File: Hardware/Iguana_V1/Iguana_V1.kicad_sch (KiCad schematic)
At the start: 112 parts, among them J1 ON OFF, J11 Conn_Coaxial, J12 Conn_Coaxial, J13 HDR-3x1, J14 HDR-3x1, J15 ds18b20, J16 SHT31, J17 HDR-2x1, J18 OLED, J19 NPK/H Sensor, J3 BAT, J4 HDR-2x1, J7 USB_B_Micro, J8 Cap. Moisture Sensor, J9 Conn_01x02, Q1 Q_PMOS_GSD, Q3 Q_Dual_NPN_NPN_BRT_E1B1C2E2B2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, SW1 SW_DIP_x02, SW2 SW_DIP_x02, SW3 SW_DIP_x02, U1 DW01, U10 RV-8803, U11 RFM95W-915S2, U12 MAX3485, U2 TP4056, U3 MT3608, U4 FS8205A, U5 AP2112K-3.3, U6 AP2112K-3.3, U7 AP2112K-3.3, U8 CH340C, U9 ESP32-WROOM-32D

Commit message: adding relay and working on pcb
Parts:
- removed H1, H2, H3, H4, H5, H6, H7, H8: MountingHole, MountingHole:MountingHole_3.2mm_M3, symbol Mechanical:MountingHole
- removed J1: ON OFF, Connector_JST:JST_XH_B2B-XH-A_1x02_P2.50mm_Vertical, symbol IoWLabsConnectors:HDR-2x1
- removed J11: Conn_Coaxial, Connector_Coaxial:SMA_Samtec_SMA-J-P-X-ST-EM1_EdgeMount, symbol Connector:Conn_Coaxial
- removed J14: HDR-3x1, Jumper:SolderJumper-3_P1.3mm_Open_RoundedPad1.0x1.5mm_NumberLabels, symbol IoWLabsConnectors:HDR-3x1
- removed JP1, JP2: SolderJumper_2_Open, Jumper:SolderJumper-2_P1.3mm_Open_RoundedPad1.0x1.5mm, symbol Jumper:SolderJumper_2_Open
- removed R16, R17: 200, Resistor_SMD:R_0603_1608Metric, symbol IoWLabs:RES
- removed R29, R30: 2.2k, Resistor_SMD:R_0603_1608Metric, symbol IoWLabs:RES
- added C6: 4.7u, Capacitor_SMD:C_0805_2012Metric, symbol IoWLabs:C
- added D12: LED, LED_SMD:LED_0603_1608Metric, symbol Device:LED
- added D13: MRA4007T3G, Diode_SMD:D_SMA, symbol Diode:MRA4007T3G
- added D14: WS2812B, LED_SMD:LED_WS2812B_PLCC4_5.0x5.0mm_P3.2mm, symbol LED:WS2812B
- added D9: D_Schottky, Diode_SMD:D_SMA, symbol Device:D_Schottky
- added J18, J19, J3: IN, Connector_JST:JST_XH_B2B-XH-A_1x02_P2.50mm_Vertical, symbol IoWLabsConnectors:HDR-2x1
- added J8: ON OFF, Jumper:SolderJumper-2_P1.3mm_Open_RoundedPad1.0x1.5mm, symbol IoWLabsConnectors:HDR-2x1
- added K1: Relay_SPDT, Relay_THT:Relay_SPDT_SANYOU_SRD_Series_Form_C, symbol Relay:Relay_SPDT
- added Q2: Q_PMOS_GSD, Package_TO_SOT_SMD:SOT-23, symbol Device:Q_PMOS_GSD
- added Q4: MMBT3904, Package_TO_SOT_SMD:SOT-23, symbol Transistor_BJT:MMBT3904
- added R14: 10K, Resistor_SMD:R_0603_1608Metric, symbol IoWLabs:RES
- added R38: 330, Resistor_SMD:R_0603_1608Metric, symbol IoWLabs:RES
- added R39: 10, Resistor_SMD:R_0603_1608Metric, symbol IoWLabs:RES
- J1: renamed from J3; footprint IoWLabsConnectors:Tb-2x1-5p-TH-V -> Connector_JST:JST_XH_B2B-XH-A_1x02_P2.50mm_Vertical
- J13: renamed from J17; footprint Connector_PinHeader_2.54mm:PinHeader_1x02_P2.54mm_Vertical -> Jumper:SolderJumper-2_P1.3mm_Open_RoundedPad1.0x1.5mm
- J2: renamed from J4; footprint Jumper:SolderJumper-2_P1.3mm_Open_RoundedPad1.0x1.5mm -> Connector_PinHeader_2.54mm:PinHeader_1x02_P2.54mm_Vertical
- J4: renamed from J8; footprint Connector_JST:JST_EH_S3B-EH_1x03_P2.50mm_Horizontal -> Connector_JST:JST_XH_B3B-XH-A_1x03_P2.50mm_Vertical
- J5: renamed from J15; footprint Connector_JST:JST_EH_S3B-EH_1x03_P2.50mm_Horizontal -> Connector_JST:JST_XH_B3B-XH-A_1x03_P2.50mm_Vertical
- J6: renamed from J16; footprint Connector_JST:JST_EH_S4B-EH_1x04_P2.50mm_Horizontal -> Connector_JST:JST_XH_B4B-XH-A_1x04_P2.50mm_Vertical
- J7: renamed from J19; footprint Connector_JST:JST_EH_S4B-EH_1x04_P2.50mm_Horizontal -> Connector_JST:JST_XH_B4B-XH-A_1x04_P2.50mm_Vertical
- renumbered C6 to C7, D5 to D4, D6 to D5, D7 to D6, D8 to D7, D4 to D8, J18 to J10, J7 to J12, J9 to J14, J10 to J15, J12 to J17, J13 to J9, R11 to R10, R12 to R11, R13 to R12, R2 to R13, R32 to R15, R36 to R16, R14 to R17, R33 to R18, R34 to R19, R3 to R2, R35 to R20, R15 to R22, R18 to R24, R19 to R25, R20 to R26, R21 to R27, R22 to R28, R23 to R29, R4 to R3, R24 to R30, R25 to R31, R26 to R32, R27 to R33, R28 to R34, R31 to R37, R5 to R4, R6 to R5, R7 to R6, R8 to R7, R9 to R8, R10 to R9, U9 to U10, U10 to U11, U11 to U12, U12 to U7, U7 to U8, U8 to U9
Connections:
- net EN_VS_S is gone; now on net EN_VDS/S: U8.3 (EN)
- net +3V3: now also D14.1 (VDD)
- net GND: now also C6.2, D14.3 (VSS), J3.1, Q4.2 (E), R14.2
- net IO0: now also SW2.3, SW2.4
- net RESET: now also SW3.3, SW3.4
- net V1: now also D8.1 (K), Q1.2 (S)
- net VS_3V3: now also D12.2 (A), R39.2
- net V_USB: now also D9.2 (A), J8.1, Q2.1 (G), R14.1; no longer C4.1, D8.2 (A), Q1.1 (G), R1.1, R13.1, U2.4 (Vcc), U2.8 (CE)
- net at U12.9 (ANT): now also J17.1 (In)
- net LORA_D1: now reaches U10.12 (IO27)
- net LORA_D1: now also U12.15 (DIO1)
- net SPI2_CLK: now reaches U10.14 (IO12)
- net SENS_M: now reaches U10.6 (IO34)
- net SENS_M: now also J4.3
- net V_EN: now reaches U10.9 (IO33)
- net V_EN: now also J9.2
- net EN_VDL renamed EN_VDS/S
- net EN_VDS/S: now also U6.3 (EN)
- removed net EN_VDL_S: J9.2, U6.3 (EN)
- net Msensor renamed RS485_TX
- net RS485_TX: now also R17.2, U7.1 (RO); no longer J4.3
- net RS_EN_CH1 renamed RS485_EN
- net RS485_EN: now also U10.26 (IO4); no longer U10.8 (IO32)
- net SD_cs renamed SD_CS
- net rfm_cs renamed LORA_CS
- net rfm_dio0 renamed LORA_D0
- net LORA_D0: now also U10.11 (IO26); no longer U10.16 (IO13)
- net rfm_dio1 renamed RBG
- net RBG: no longer U12.15 (DIO1)
- net rfm_rst renamed LORA_RST
- net LORA_RST: now also U10.10 (IO25); no longer U10.26 (IO4)
- net rx_aux renamed RS485_RX
- net RS485_RX: now also U10.28 (IO17); no longer U10.10 (IO25)
- net spi_clk renamed SPI1_CLK
- net spi_miso renamed SPI1_MISO
- net spi_mosi renamed SPI1_MOSI
- net temp renamed SENS_TEMP
- net SENS_TEMP: now also U10.8 (IO32); no longer U10.28 (IO17)
- removed net tx_aux: R17.2, U10.11 (IO26), U7.1 (RO)
- new net: D13.2 (A), K1.2 (A2), Q4.3 (C), R38.1
- new net: D13.1 (K), K1.5 (A1), R39.1
- new net: D12.1 (K), R38.2
- new net PUMP: U10.16 (IO13)
- new net PUMP_IN+: J18.2, K1.1 (11)
- new net PUMP_IN-: J18.1, J19.1
- new net PUMP_OUT+: J19.2, K1.3 (14)
- new net RGB: D14.4 (DIN)
- new net VIN_5V: C6.1, J3.2, Q2.3 (D)
- new net Vin_main: C4.1, D8.2 (A), D9.1 (K), J8.2, Q1.1 (G), Q2.2 (S), R1.1, R13.1, U2.4 (Vcc), U2.8 (CE)
- no-connect marks 12 -> 13
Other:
- note added: "PUMP"
- note added: "Power IN"
- note added: "Tabla de pines ---------------- SPI1_MOSI - GPIO23 SPI1_MISO - GPIO19 SPI1_SCK - GPIO18 CS_SD - GPIO5 RGB - GPIO13 - GPIO12 PUMP - GPIO14 LORA_CS - GPIO15 LORA_RST - GPIO25 LORA_D0 - GPIO26 LORA_D1 - GPIO27 I2C_SDA - GPIO21 I2C_SCL - GPIO22 RS485_TX - GPIO16 RS485_Rx - GPIO17 RS485_EN - GPIO4 SENS_M - GPIO34 SENS_TEMP - GPIO32 EN_VDL - GPIO33 EN_VS - GPIO33"
- note removed: "Tabla de pines ---------------- SPI_MOSI - GPIO23 SPI_MISO - GPIO19 SPI_SCK - GPIO18 CS_LORA - GPIO15 CS_SD - GPIO5 I2C_SDA - GPIO21 I2C_SCL - GPIO22 EN_VDL - EN_VS -"

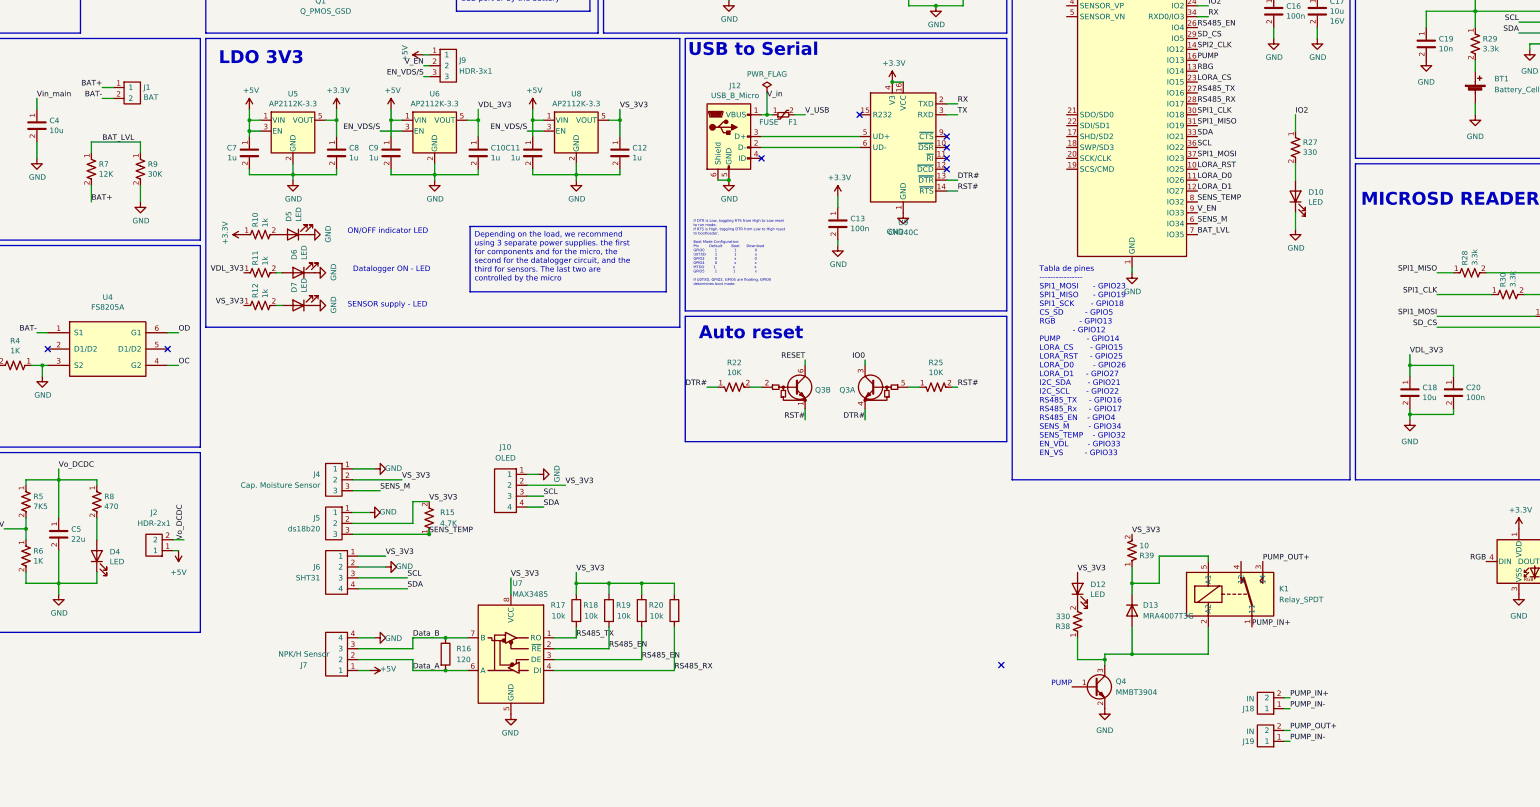
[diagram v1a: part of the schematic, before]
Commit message: replace relay. working on pcb
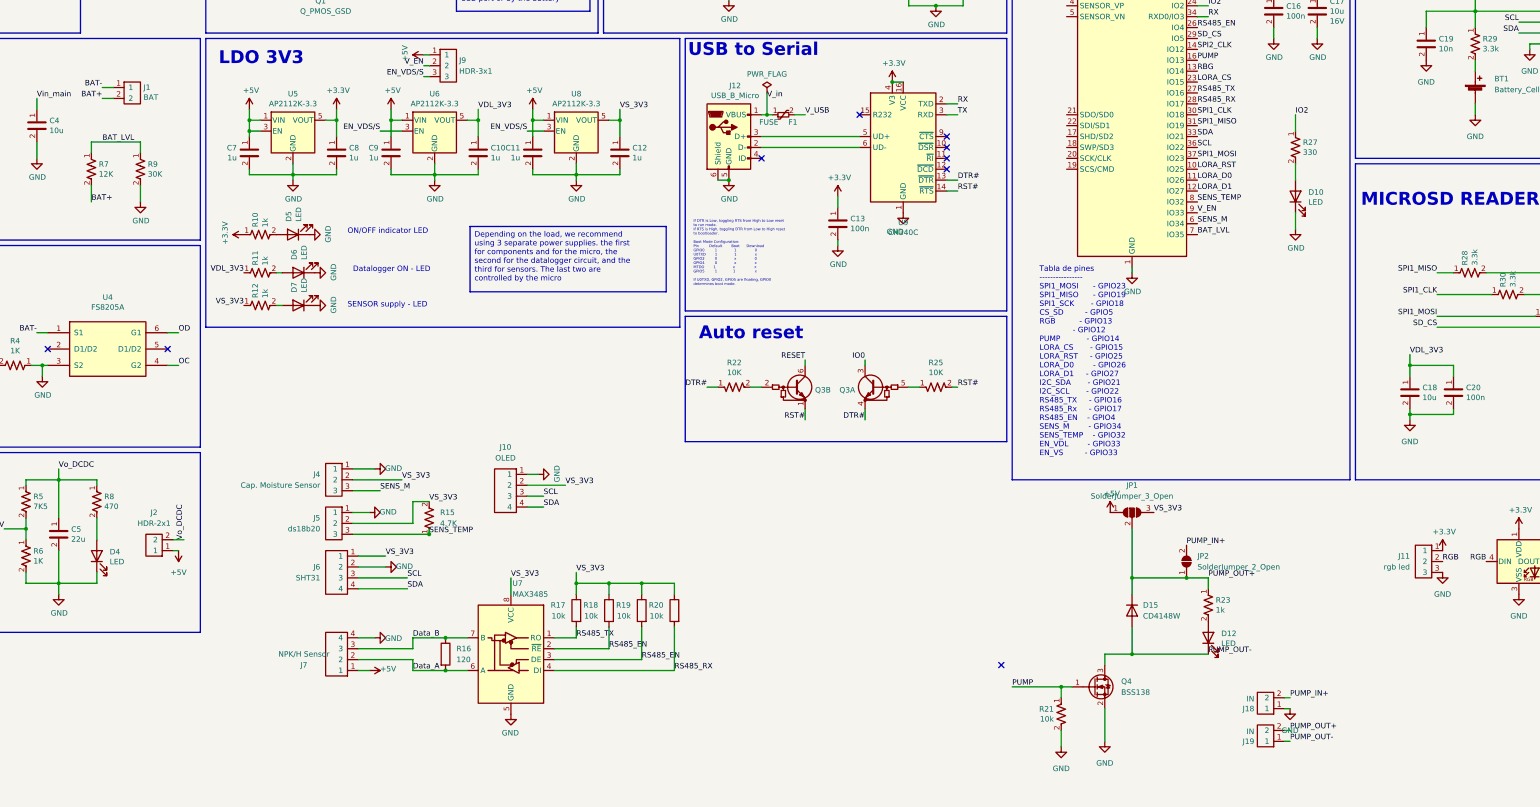
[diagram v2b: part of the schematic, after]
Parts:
- removed D13: MRA4007T3G, Diode_SMD:D_SMA, symbol Diode:MRA4007T3G
- removed K1: Relay_SPDT, Relay_THT:Relay_SPDT_SANYOU_SRD_Series_Form_C, symbol Relay:Relay_SPDT
- removed Q4: MMBT3904, Package_TO_SOT_SMD:SOT-23, symbol Transistor_BJT:MMBT3904
- removed R38: 330, Resistor_SMD:R_0603_1608Metric, symbol IoWLabs:RES
- removed R39: 10, Resistor_SMD:R_0603_1608Metric, symbol IoWLabs:RES
- added D15: CD4148W, Diode_SMD:D_0805_2012Metric, symbol Diode:CD4148W
- added J11: rgb led, Connector_JST:JST_XH_B3B-XH-A_1x03_P2.50mm_Vertical, symbol IoWLabsConnectors:HDR-3x1
- added JP1: SolderJumper_3_Open, Jumper:SolderJumper-3_P1.3mm_Open_RoundedPad1.0x1.5mm, symbol Jumper:SolderJumper_3_Open
- added JP2: SolderJumper_2_Open, Jumper:SolderJumper-2_P1.3mm_Open_RoundedPad1.0x1.5mm, symbol Jumper:SolderJumper_2_Open
- added Q4: BSS138, Package_TO_SOT_SMD:SOT-23, symbol Transistor_FET:BSS138
- added R21: 10k, Resistor_SMD:R_0603_1608Metric, symbol IoWLabs:RES
- added R23: 1k, Resistor_SMD:R_0603_1608Metric, symbol IoWLabs:RES
- J10: footprint Connector_JST:JST_EH_B4B-EH-A_1x04_P2.50mm_Vertical -> Connector_JST:JST_XH_B4B-XH-A_1x04_P2.50mm_Vertical
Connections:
- net +3V3: now also J11.1
- net +5V: now also JP1.1 (A)
- net BAT+: now also J1.2; no longer J1.1
- net BAT-: now also J1.1; no longer J1.2
- net GND: now also J18.1, J11.3, Q4.2 (S), R21.2
- net PUMP: now also Q4.1 (G), R21.1
- net PUMP_IN+: now also JP2.2 (B)
- net PUMP_OUT+: now also D15.1 (K), JP1.2 (C), JP2.1 (A), R23.1
- net RGB: now also J11.2
- net VS_3V3: now also JP1.3 (B); no longer D12.2 (A)
- net PUMP_OUT-: now reaches D12.1 (K)
- net PUMP_OUT-: now also J19.1, D15.2 (A), Q4.3 (D)
- removed net PUMP_IN-: J18.1, J19.1
- new net: D12.2 (A), R23.2
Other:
- note removed: "PUMP"

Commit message: pcb finished
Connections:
- net RBG is gone; now on net RGB: U10.13 (IO14)
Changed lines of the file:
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@@
     (effects (font (size 1.27 1.27)) (justify right bottom))
   )
-  (label "RBG" (at 359.41 66.04 0) (fields_autoplaced)
+  (label "RGB" (at 359.41 66.04 0) (fields_autoplaced)
     (effects (font (size 1.27 1.27)) (justify left bottom))
   )
